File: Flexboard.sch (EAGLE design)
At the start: 452 parts, among them J1 USB4105-GF-A, SW1 1825910-7, U1 MK22FX512AVLQ12, U2 NCP1117ST33T3G, Y1 ABM3B-8.000MHZ-B2-T, Y2 ABS07-32.768KHZ-T

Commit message: added four media keys
added four additional media keys to board, and renumbered keys to
perserve correct numbering sequence.

Signed-off-by: Daniel DeGrasse <daniel@degrasse.com>
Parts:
- added D147, D148, D149: BAS16LT3G, BAS16LT3G:BAS16LT3G
- added D150: UPS115UE3/TR7, UPS115UE3-TR7:UPS115UE3/TR7
- added KEY_146, KEY_147, KEY_148, KEY_149: CHERRY-MX-LED, cherrymx:CHERRY-MX-LED
- D146: value UPS115UE3/TR7 -> BAS16LT3G; device UPS115UE3-TR7:UPS115UE3/TR7 -> BAS16LT3G:BAS16LT3G
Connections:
- new net N$155: D149.C, KEY_149.SW2
- new net N$159: D146.C, KEY_146.SW2
- new net N$161: D148.C, KEY_148.SW2
- new net N$165: D147.C, KEY_147.SW2
- net COL_10: now also KEY_100.SW1, KEY_122.SW1, KEY_54.SW1, KEY_77.SW1; no longer KEY_118.SW1, KEY_50.SW1, KEY_73.SW1, KEY_96.SW1
- net COL_11: now also KEY_101.SW1, KEY_123.SW1, KEY_55.SW1, KEY_78.SW1; no longer KEY_119.SW1, KEY_51.SW1, KEY_74.SW1, KEY_97.SW1
- net COL_12: now also KEY_102.SW1, KEY_124.SW1, KEY_139.SW1, KEY_56.SW1, KEY_79.SW1; no longer KEY_120.SW1, KEY_135.SW1, KEY_52.SW1, KEY_75.SW1, KEY_98.SW1
- net COL_13: now also KEY_103.SW1, KEY_125.SW1, KEY_140.SW1, KEY_57.SW1, KEY_80.SW1; no longer KEY_121.SW1, KEY_136.SW1, KEY_53.SW1, KEY_76.SW1, KEY_99.SW1
- net COL_14: now also KEY_104.SW1, KEY_141.SW1, KEY_58.SW1, KEY_81.SW1; no longer KEY_100.SW1, KEY_137.SW1, KEY_54.SW1, KEY_77.SW1
- net COL_15: now also KEY_59.SW1, KEY_82.SW1; no longer KEY_55.SW1, KEY_78.SW1
- net COL_17: now also KEY_105.SW1, KEY_126.SW1, KEY_142.SW1, KEY_60.SW1, KEY_83.SW1; no longer KEY_101.SW1, KEY_122.SW1, KEY_138.SW1, KEY_56.SW1, KEY_79.SW1
- net COL_18: now also KEY_106.SW1, KEY_127.SW1, KEY_143.SW1, KEY_61.SW1, KEY_84.SW1; no longer KEY_102.SW1, KEY_123.SW1, KEY_139.SW1, KEY_57.SW1, KEY_80.SW1
- net COL_19: now also KEY_107.SW1, KEY_128.SW1, KEY_144.SW1, KEY_62.SW1, KEY_85.SW1; no longer KEY_103.SW1, KEY_124.SW1, KEY_140.SW1, KEY_58.SW1, KEY_81.SW1
- net COL_1{SB}: now also KEY_113.SW1, KEY_133.SW1, KEY_45.SW1, KEY_68.SW1, KEY_91.SW1; no longer KEY_109.SW1, KEY_129.SW1, KEY_41.SW1, KEY_64.SW1, KEY_87.SW1
- net COL_20: now also KEY_108.SW1, KEY_129.SW1, KEY_145.SW1, KEY_63.SW1, KEY_86.SW1; no longer KEY_104.SW1, KEY_125.SW1, KEY_141.SW1, KEY_59.SW1, KEY_82.SW1
- net COL_21: now also KEY_109.SW1, KEY_130.SW1, KEY_146.SW1, KEY_41.SW1, KEY_64.SW1, KEY_87.SW1; no longer KEY_105.SW1, KEY_126.SW1, KEY_142.SW1, KEY_60.SW1, KEY_83.SW1
- net COL_22: now also KEY_110.SW1, KEY_131.SW1, KEY_147.SW1, KEY_42.SW1, KEY_65.SW1, KEY_88.SW1; no longer KEY_106.SW1, KEY_127.SW1, KEY_143.SW1, KEY_61.SW1, KEY_84.SW1
- net COL_23: now also KEY_111.SW1, KEY_132.SW1, KEY_148.SW1, KEY_43.SW1, KEY_66.SW1, KEY_89.SW1; no longer KEY_107.SW1, KEY_128.SW1, KEY_144.SW1, KEY_62.SW1, KEY_85.SW1
- net COL_24: now also KEY_112.SW1, KEY_149.SW1, KEY_44.SW1, KEY_67.SW1, KEY_90.SW1; no longer KEY_108.SW1, KEY_145.SW1, KEY_63.SW1, KEY_86.SW1
- net COL_2{SB}: now also KEY_114.SW1, KEY_134.SW1, KEY_46.SW1, KEY_69.SW1, KEY_92.SW1; no longer KEY_110.SW1, KEY_130.SW1, KEY_42.SW1, KEY_65.SW1, KEY_88.SW1
- net COL_3: now also KEY_115.SW1, KEY_135.SW1, KEY_47.SW1, KEY_70.SW1, KEY_93.SW1; no longer KEY_111.SW1, KEY_131.SW1, KEY_43.SW1, KEY_66.SW1, KEY_89.SW1
- net COL_4: now also KEY_116.SW1, KEY_136.SW1, KEY_48.SW1, KEY_71.SW1, KEY_94.SW1; no longer KEY_112.SW1, KEY_132.SW1, KEY_44.SW1, KEY_67.SW1, KEY_90.SW1
- net COL_5: now also KEY_117.SW1, KEY_137.SW1, KEY_49.SW1, KEY_72.SW1, KEY_95.SW1; no longer KEY_113.SW1, KEY_133.SW1, KEY_45.SW1, KEY_68.SW1, KEY_91.SW1
- net COL_6: now also KEY_118.SW1, KEY_50.SW1, KEY_73.SW1, KEY_96.SW1; no longer KEY_114.SW1, KEY_46.SW1, KEY_69.SW1, KEY_92.SW1
- net COL_7: now also KEY_119.SW1, KEY_51.SW1, KEY_74.SW1, KEY_97.SW1; no longer KEY_115.SW1, KEY_47.SW1, KEY_70.SW1, KEY_93.SW1
- net COL_8: now also KEY_120.SW1, KEY_138.SW1, KEY_52.SW1, KEY_75.SW1, KEY_98.SW1; no longer KEY_116.SW1, KEY_134.SW1, KEY_48.SW1, KEY_71.SW1, KEY_94.SW1
- net COL_9: now also KEY_121.SW1, KEY_53.SW1, KEY_76.SW1, KEY_99.SW1; no longer KEY_117.SW1, KEY_49.SW1, KEY_72.SW1, KEY_95.SW1
- net LED_COL_10: now also KEY_100.LED-, KEY_122.LED-, KEY_54.LED-, KEY_77.LED-; no longer KEY_118.LED-, KEY_50.LED-, KEY_73.LED-, KEY_96.LED-
- net LED_COL_11: now also KEY_101.LED-, KEY_123.LED-, KEY_55.LED-, KEY_78.LED-; no longer KEY_119.LED-, KEY_51.LED-, KEY_74.LED-, KEY_97.LED-
- net LED_COL_12: now also KEY_102.LED-, KEY_124.LED-, KEY_139.LED-, KEY_56.LED-, KEY_79.LED-; no longer KEY_120.LED-, KEY_135.LED-, KEY_52.LED-, KEY_75.LED-, KEY_98.LED-
- net LED_COL_13: now also KEY_103.LED-, KEY_125.LED-, KEY_140.LED-, KEY_57.LED-, KEY_80.LED-; no longer KEY_121.LED-, KEY_136.LED-, KEY_53.LED-, KEY_76.LED-, KEY_99.LED-
- net LED_COL_14: now also KEY_104.LED-, KEY_141.LED-, KEY_58.LED-, KEY_81.LED-; no longer KEY_100.LED-, KEY_137.LED-, KEY_54.LED-, KEY_77.LED-
- net LED_COL_15: now also KEY_59.LED-, KEY_82.LED-; no longer KEY_55.LED-, KEY_78.LED-
- net LED_COL_17: now also KEY_105.LED-, KEY_126.LED-, KEY_142.LED-, KEY_60.LED-, KEY_83.LED-; no longer KEY_101.LED-, KEY_122.LED-, KEY_138.LED-, KEY_56.LED-, KEY_79.LED-
- net LED_COL_18: now also KEY_106.LED-, KEY_127.LED-, KEY_143.LED-, KEY_61.LED-, KEY_84.LED-; no longer KEY_102.LED-, KEY_123.LED-, KEY_139.LED-, KEY_57.LED-, KEY_80.LED-
- net LED_COL_19: now also KEY_107.LED-, KEY_128.LED-, KEY_144.LED-, KEY_62.LED-, KEY_85.LED-; no longer KEY_103.LED-, KEY_124.LED-, KEY_140.LED-, KEY_58.LED-, KEY_81.LED-
- net LED_COL_1{SB}: now also KEY_113.LED-, KEY_133.LED-, KEY_45.LED-, KEY_68.LED-, KEY_91.LED-; no longer KEY_109.LED-, KEY_129.LED-, KEY_41.LED-, KEY_64.LED-, KEY_87.LED-
- net LED_COL_20: now also KEY_108.LED-, KEY_129.LED-, KEY_145.LED-, KEY_63.LED-, KEY_86.LED-; no longer KEY_104.LED-, KEY_125.LED-, KEY_141.LED-, KEY_59.LED-, KEY_82.LED-
- net LED_COL_21: now also KEY_109.LED-, KEY_130.LED-, KEY_146.LED-, KEY_41.LED-, KEY_64.LED-, KEY_87.LED-; no longer KEY_105.LED-, KEY_126.LED-, KEY_142.LED-, KEY_60.LED-, KEY_83.LED-
- net LED_COL_22: now also KEY_110.LED-, KEY_131.LED-, KEY_147.LED-, KEY_42.LED-, KEY_65.LED-, KEY_88.LED-; no longer KEY_106.LED-, KEY_127.LED-, KEY_143.LED-, KEY_61.LED-, KEY_84.LED-
- net LED_COL_23: now also KEY_111.LED-, KEY_132.LED-, KEY_148.LED-, KEY_43.LED-, KEY_66.LED-, KEY_89.LED-; no longer KEY_107.LED-, KEY_128.LED-, KEY_144.LED-, KEY_62.LED-, KEY_85.LED-
- net LED_COL_24: now also KEY_112.LED-, KEY_149.LED-, KEY_44.LED-, KEY_67.LED-, KEY_90.LED-; no longer KEY_108.LED-, KEY_145.LED-, KEY_63.LED-, KEY_86.LED-
- net LED_COL_2{SB}: now also KEY_114.LED-, KEY_134.LED-, KEY_46.LED-, KEY_69.LED-, KEY_92.LED-; no longer KEY_110.LED-, KEY_130.LED-, KEY_42.LED-, KEY_65.LED-, KEY_88.LED-
- net LED_COL_3: now also KEY_115.LED-, KEY_135.LED-, KEY_47.LED-, KEY_70.LED-, KEY_93.LED-; no longer KEY_111.LED-, KEY_131.LED-, KEY_43.LED-, KEY_66.LED-, KEY_89.LED-
- net LED_COL_4: now also KEY_116.LED-, KEY_136.LED-, KEY_48.LED-, KEY_71.LED-, KEY_94.LED-; no longer KEY_112.LED-, KEY_132.LED-, KEY_44.LED-, KEY_67.LED-, KEY_90.LED-
- net LED_COL_5: now also KEY_117.LED-, KEY_49.LED-, KEY_72.LED-, KEY_95.LED-; no longer KEY_113.LED-, KEY_45.LED-, KEY_68.LED-, KEY_91.LED-
- net LED_COL_6: now also KEY_118.LED-, KEY_50.LED-, KEY_73.LED-, KEY_96.LED-; no longer KEY_114.LED-, KEY_46.LED-, KEY_69.LED-, KEY_92.LED-
- net LED_COL_7: now also KEY_119.LED-, KEY_51.LED-, KEY_74.LED-, KEY_97.LED-; no longer KEY_115.LED-, KEY_47.LED-, KEY_70.LED-, KEY_93.LED-
- net LED_COL_8: now also KEY_120.LED-, KEY_138.LED-, KEY_52.LED-, KEY_75.LED-, KEY_98.LED-; no longer KEY_116.LED-, KEY_134.LED-, KEY_48.LED-, KEY_71.LED-, KEY_94.LED-
- net LED_COL_9: now also KEY_121.LED-, KEY_53.LED-, KEY_76.LED-, KEY_99.LED-; no longer KEY_117.LED-, KEY_49.LED-, KEY_72.LED-, KEY_95.LED-
- net LED_ROW_2{SB}: now also KEY_41.LED+, KEY_42.LED+, KEY_43.LED+, KEY_44.LED+
- net LED_ROW_3: now also KEY_45.LED+, KEY_46.LED+; no longer KEY_41.LED+, KEY_42.LED+
- net LED_ROW_3{SB}: now also KEY_60.LED+, KEY_61.LED+, KEY_62.LED+, KEY_63.LED+; no longer KEY_43.LED+, KEY_44.LED+, KEY_45.LED+, KEY_46.LED+
- net LED_ROW_4: now also KEY_68.LED+, KEY_69.LED+; no longer KEY_64.LED+, KEY_65.LED+
- net LED_ROW_4{SB}: now also KEY_83.LED+, KEY_84.LED+, KEY_85.LED+, KEY_86.LED+; no longer KEY_66.LED+, KEY_67.LED+, KEY_68.LED+, KEY_69.LED+
- net LED_ROW_5: now also KEY_91.LED+, KEY_92.LED+; no longer KEY_87.LED+, KEY_88.LED+
- net LED_ROW_5{SB}: now also KEY_105.LED+, KEY_106.LED+, KEY_107.LED+, KEY_108.LED+; no longer KEY_89.LED+, KEY_90.LED+, KEY_91.LED+, KEY_92.LED+
- net LED_ROW_6: now also KEY_113.LED+, KEY_114.LED+; no longer KEY_109.LED+, KEY_110.LED+
- net LED_ROW_6{SB}: now also KEY_126.LED+, KEY_127.LED+, KEY_128.LED+, KEY_129.LED+; no longer KEY_111.LED+, KEY_112.LED+, KEY_113.LED+, KEY_114.LED+
- net LED_ROW_7: now also KEY_133.LED+, KEY_134.LED+; no longer KEY_129.LED+, KEY_130.LED+
- net LED_ROW_7{SB}: now also KEY_142.LED+, KEY_143.LED+, KEY_144.LED+, KEY_145.LED+; no longer KEY_131.LED+, KEY_132.LED+, KEY_133.LED+, KEY_134.LED+
- net N$103: now also D109.A, D110.A, D111.A, D112.A; no longer D105.A, D106.A, D107.A, D108.A
- net N$124: now also D130.A, D131.A, D132.A; no longer D126.A, D127.A, D128.A
- net N$151: now also D146.A, D147.A, D148.A, D149.A; no longer D142.A, D143.A, D144.A, D145.A
- net N$170: now also KEY_64.LED+, KEY_65.LED+, KEY_66.LED+, KEY_67.LED+; no longer KEY_60.LED+, KEY_61.LED+, KEY_62.LED+, KEY_63.LED+
- net N$173: now also KEY_87.LED+, KEY_88.LED+, KEY_89.LED+, KEY_90.LED+; no longer KEY_83.LED+, KEY_84.LED+, KEY_85.LED+, KEY_86.LED+
- net N$179: now also KEY_109.LED+, KEY_110.LED+, KEY_111.LED+, KEY_112.LED+; no longer KEY_105.LED+, KEY_106.LED+, KEY_107.LED+, KEY_108.LED+
- net N$182: now also KEY_130.LED+, KEY_131.LED+, KEY_132.LED+; no longer KEY_126.LED+, KEY_127.LED+, KEY_128.LED+
- net N$185: now also KEY_146.LED+, KEY_147.LED+, KEY_148.LED+, KEY_149.LED+; no longer KEY_142.LED+, KEY_143.LED+, KEY_144.LED+, KEY_145.LED+
- net N$65: now also D64.A, D65.A, D66.A, D67.A; no longer D60.A, D61.A, D62.A, D63.A
- net N$79: now also D87.A, D88.A, D89.A, D90.A; no longer D83.A, D84.A, D85.A, D86.A
- net ROW_2{SB}: now also D41.A, D42.A, D43.A, D44.A
- net ROW_3: now also D45.A, D46.A; no longer D41.A, D42.A
- net ROW_3{SB}: now also D60.A, D61.A, D62.A, D63.A; no longer D43.A, D44.A, D45.A, D46.A
- net ROW_4: now also D68.A, D69.A; no longer D64.A, D65.A
- net ROW_4{SB}: now also D83.A, D84.A, D85.A, D86.A; no longer D66.A, D67.A, D68.A, D69.A
- net ROW_5: now also D91.A, D92.A; no longer D87.A, D88.A
- net ROW_5{SB}: now also D105.A, D106.A, D107.A, D108.A; no longer D89.A, D90.A, D91.A, D92.A
- net ROW_6: now also D113.A, D114.A; no longer D109.A, D110.A
- net ROW_6{SB}: now also D126.A, D127.A, D128.A, D129.A; no longer D111.A, D112.A, D113.A, D114.A
- net ROW_7: now also D133.A, D134.A; no longer D129.A, D130.A
- net ROW_7{SB}: now also D142.A, D143.A, D144.A, D145.A; no longer D131.A, D132.A, D133.A, D134.A
- net VLDO_5V5: now also D150.P$1; no longer D146.P$1
- net VSYS_5V5: now also D150.P$2; no longer D146.P$2
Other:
- moved on the sheet: D100, D101, D102, D103, D104, D105, D106, D107, D108, D109, D110, D111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

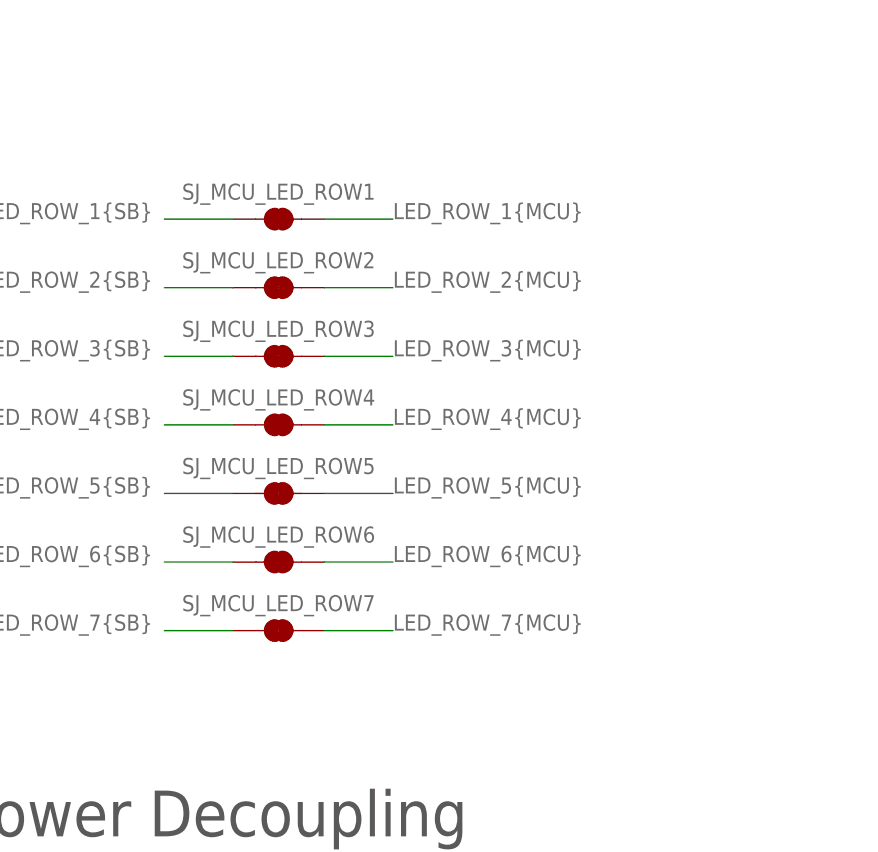
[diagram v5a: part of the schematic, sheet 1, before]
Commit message: added current limiting resistors to LED rows
current limit resistors should limit LED network to 10mA across each
LED, for a total of roughly 70mA sourced from the chip.

Signed-off-by: Daniel DeGrasse <daniel@degrasse.com>
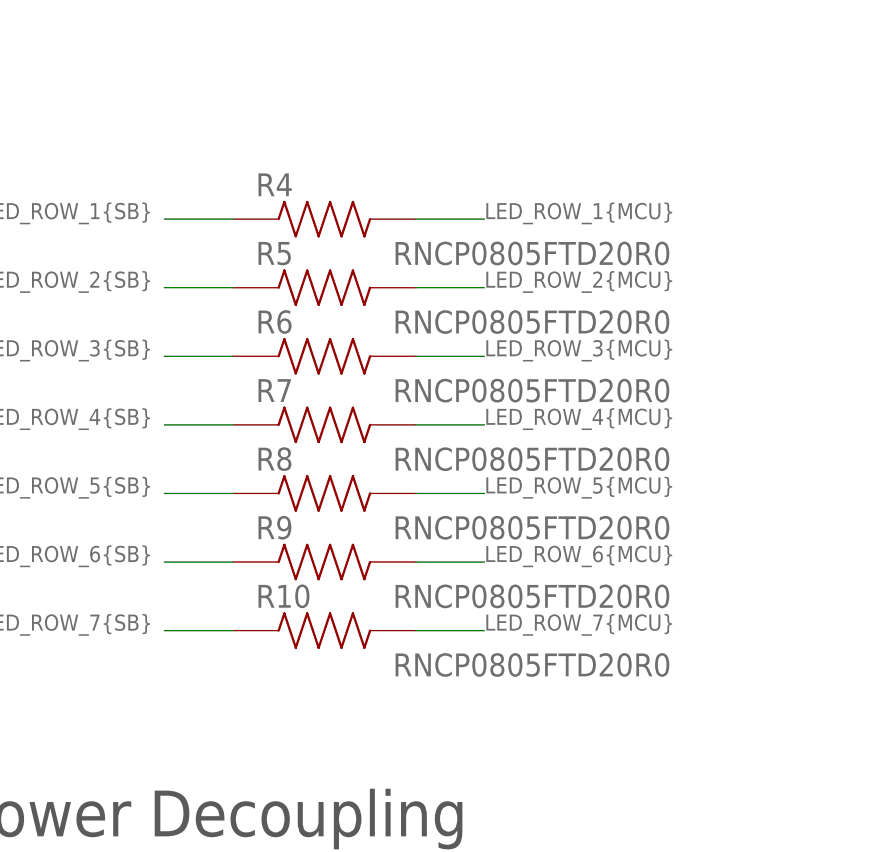
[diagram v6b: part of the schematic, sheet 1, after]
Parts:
- removed SJ_MCU_LED_ROW1, SJ_MCU_LED_ROW2, SJ_MCU_LED_ROW3, SJ_MCU_LED_ROW4, SJ_MCU_LED_ROW5, SJ_MCU_LED_ROW6, SJ_MCU_LED_ROW7: JUMPER-SMT_2_NC_TRACE_NO-SILK, SparkFun-Jumpers:JUMPER-SMT_2_NC_TRACE_NO-SILK
- added R10, R4, R5, R6, R7, R8, R9: RNCP0805FTD20R0, RNCP0805FTD20R0:RNCP0805FTD20R0
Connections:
- net LED_ROW_1{MCU}: now also R4.2; no longer SJ_MCU_LED_ROW1.2
- net LED_ROW_1{SB}: now also R4.1; no longer SJ_MCU_LED_ROW1.1
- net LED_ROW_2{MCU}: now also R5.2; no longer SJ_MCU_LED_ROW2.2
- net LED_ROW_2{SB}: now also R5.1; no longer SJ_MCU_LED_ROW2.1
- net LED_ROW_3{MCU}: now also R6.2; no longer SJ_MCU_LED_ROW3.2
- net LED_ROW_3{SB}: now also R6.1; no longer SJ_MCU_LED_ROW3.1
- net LED_ROW_4{MCU}: now also R7.2; no longer SJ_MCU_LED_ROW4.2
- net LED_ROW_4{SB}: now also R7.1; no longer SJ_MCU_LED_ROW4.1
- net LED_ROW_5{MCU}: now also R8.2; no longer SJ_MCU_LED_ROW5.2
- net LED_ROW_5{SB}: now also R8.1; no longer SJ_MCU_LED_ROW5.1
- net LED_ROW_6{MCU}: now also R9.2; no longer SJ_MCU_LED_ROW6.2
- net LED_ROW_6{SB}: now also R9.1; no longer SJ_MCU_LED_ROW6.1
- net LED_ROW_7{MCU}: now also R10.2; no longer SJ_MCU_LED_ROW7.2
- net LED_ROW_7{SB}: now also R10.1; no longer SJ_MCU_LED_ROW7.1

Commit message: cleaned up name locations on board
cleaned up name locations on board silkscreen to ensure that there will
not be overlap between board printing and solder pads

Signed-off-by: Daniel DeGrasse <daniel@degrasse.com>
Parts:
- renumbered U$1 to J2
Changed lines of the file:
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@@
 <part name="SJ_MCU_LED_COL24" library="SparkFun-Jumpers" deviceset="JUMPER-SMT_2_NC_TRACE" device="_NO-SILK" package3d_urn="urn:adsk.eagle:package:39286/1"/>
 <part name="J1" library="USB4105-GF-A" deviceset="USB4105-GF-A" device=""/>
-<part name="U$1" library="GRPB052VWQS-RC" deviceset="GRPB052VWQS-RC" device=""/>
+<part name="J2" library="GRPB052VWQS-RC" deviceset="GRPB052VWQS-RC" device=""/>
 <part name="R1" library="CRGCQ1206J10K" deviceset="CRGCQ1206J10K" device="" value="10k"/>
 <part name="C1" library="C1206C102K1RACAUTO" deviceset="C1206C102K1RACAUTO" device="" value="1000pF"/>
@@
 <attribute name="VALUE" x="-241.3" y="76.2" size="1.778" layer="96"/>
 </instance>
-<instance part="U$1" gate="G$1" x="264.16" y="71.12" smashed="yes">
+<instance part="J2" gate="G$1" x="264.16" y="71.12" smashed="yes">
 <attribute name="NAME" x="253.9902" y="85.1034" size="1.779709375" layer="95"/>
 <attribute name="VALUE" x="274.3305" y="54.5929" size="1.779840625" layer="96" rot="R180"/>
@@
 </segment>
 <segment>
-<pinref part="U$1" gate="G$1" pin="VCC"/>
+<pinref part="J2" gate="G$1" pin="VCC"/>
 <wire x1="248.92" y1="81.28" x2="241.3" y2="81.28" width="0.1524" layer="91"/>
 <label x="231.14" y="81.28" size="1.778" layer="95"/>
@@
 </segment>
 <segment>
-<pinref part="U$1" gate="G$1" pin="GND"/>
+<pinref part="J2" gate="G$1" pin="GND"/>
 <wire x1="248.92" y1="76.2" x2="241.3" y2="76.2" width="0.1524" layer="91"/>
 <label x="236.22" y="76.2" size="1.778" layer="95"/>
 </segment>
 <segment>
-<pinref part="U$1" gate="G$1" pin="GND2"/>
+<pinref part="J2" gate="G$1" pin="GND2"/>
 <wire x1="248.92" y1="71.12" x2="241.3" y2="71.12" width="0.1524" layer="91"/>
 <label x="236.22" y="71.12" size="1.778" layer="95"/>
@@
 </segment>
 <segment>
-<pinref part="U$1" gate="G$1" pin="TCK"/>
+<pinref part="J2" gate="G$1" pin="TCK"/>
 <wire x1="279.4" y1="73.66" x2="284.48" y2="73.66" width="0.1524" layer="91"/>
 <label x="284.48" y="73.66" size="1.778" layer="95"/>
@@
 </segment>
 <segment>
-<pinref part="U$1" gate="G$1" pin="TDI"/>
+<pinref part="J2" gate="G$1" pin="TDI"/>
 <wire x1="279.4" y1="63.5" x2="284.48" y2="63.5" width="0.1524" layer="91"/>
 <label x="284.48" y="63.5" size="1.778" layer="95"/>
@@
 </segment>
 <segment>
-<pinref part="U$1" gate="G$1" pin="TDO"/>
+<pinref part="J2" gate="G$1" pin="TDO"/>
 <wire x1="279.4" y1="68.58" x2="284.48" y2="68.58" width="0.1524" layer="91"/>
 <label x="284.48" y="68.58" size="1.778" layer="95"/>
@@
 </segment>
 <segment>
-<pinref part="U$1" gate="G$1" pin="TMS"/>
+<pinref part="J2" gate="G$1" pin="TMS"/>
 <wire x1="279.4" y1="78.74" x2="284.48" y2="78.74" width="0.1524" layer="91"/>
 <label x="284.48" y="78.74" size="1.778" layer="95"/>
@@
 </segment>
 <segment>
-<pinref part="U$1" gate="G$1" pin="NRESET"/>
+<pinref part="J2" gate="G$1" pin="NRESET"/>
 <label x="284.48" y="58.42" size="1.778" layer="95"/>
 <wire x1="279.4" y1="58.42" x2="325.12" y2="58.42" width="0.1524" layer="91"/>

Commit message: Fixed ERC errors
Fixed valid ERC errors, and approved remaining overlap warnings as
nonissues

Signed-off-by: Daniel DeGrasse <daniel@degrasse.com>
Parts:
- added C15: 1000pF, C1206C102K1RACAUTO:C1206C102K1RACAUTO
- added R11: 10k, CRGCQ1206J10K:CRGCQ1206J10K
- renumbered SJ__LED_R4_0 to SJ_LED_R4_0
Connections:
- net GND: now also C15.2
- net NMI: now also C15.1, R11.1
- net VDD_3V3: now also R11.2
